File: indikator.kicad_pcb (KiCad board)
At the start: 2 copper layers, 125 x 52.5 mm, 104 parts, among them J1 Conn_01x02, Q1 AO3400A, Q10 AO3400A, Q11 AO3400A, Q12 AO3400A, Q13 AO3400A, Q14 AO3400A, Q15 AO3400A, Q16 AO3400A, Q17 AO3400A, Q18 AO3400A, Q19 AO3400A, Q2 AO3400A, Q20 AO3400A, Q21 AO3400A, Q22 AO3400A, Q23 AO3400A, Q24 AO3400A, Q3 AO3400A, Q4 AO3400A, Q5 AO3400A, Q6 AO3400A, Q7 AO3400A, Q8 AO3400A, Q9 AO3400A, U1 XIAO-ESP32-C3-SMD, U2 74HC595, U3 74HC595, U4 74HC595

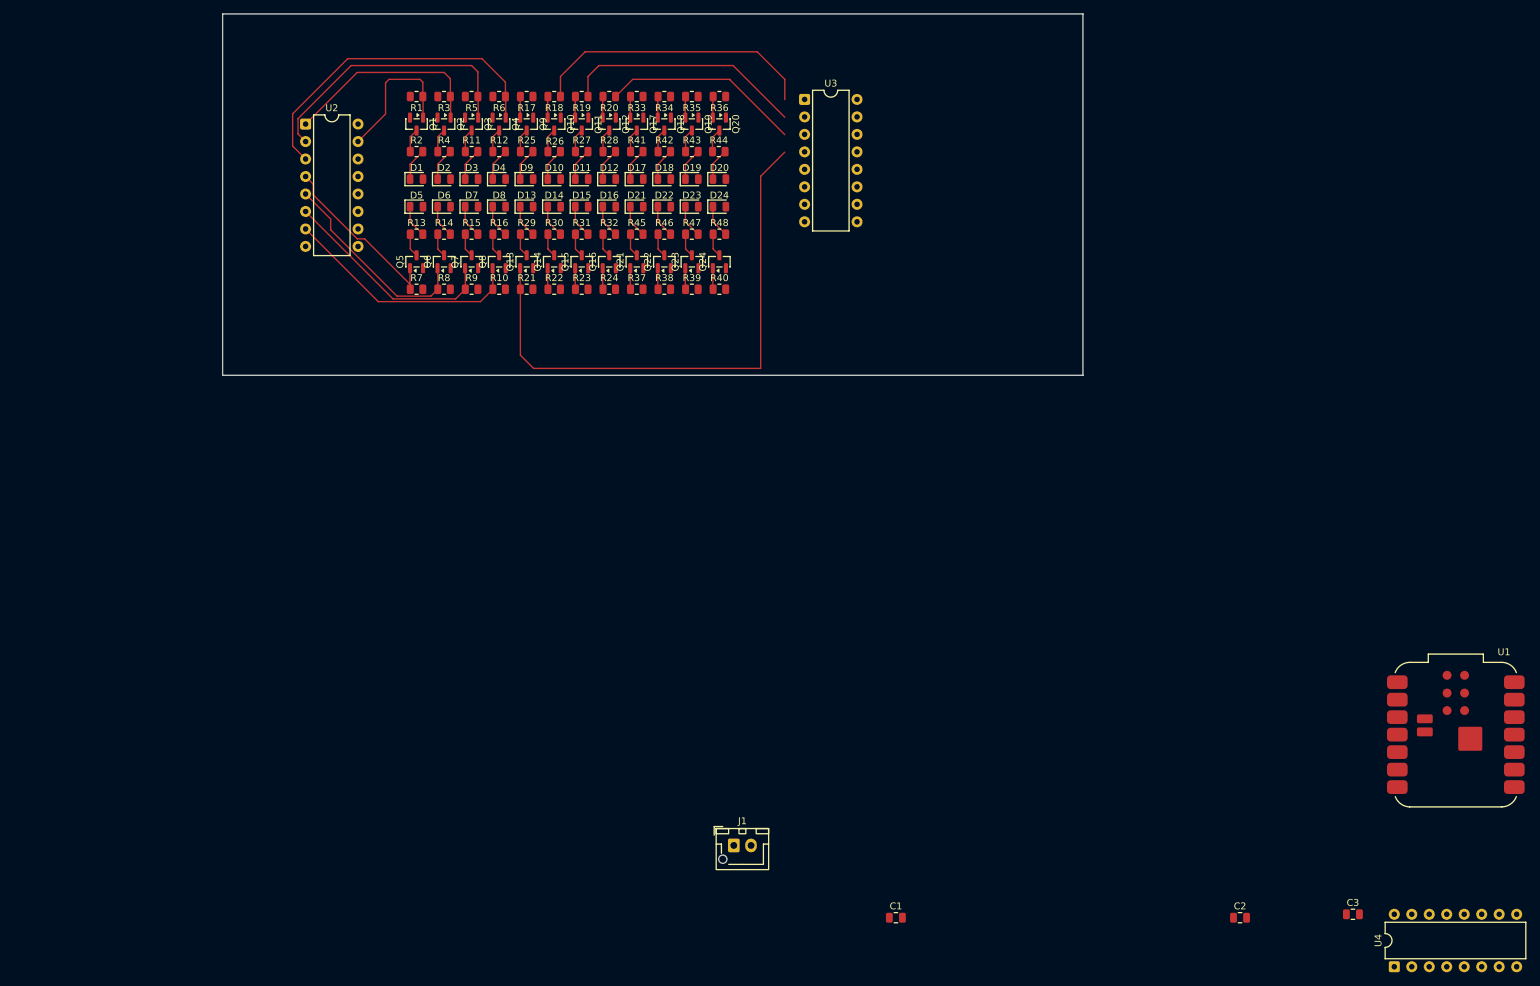
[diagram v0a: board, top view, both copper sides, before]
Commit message: LOTS of routing progress
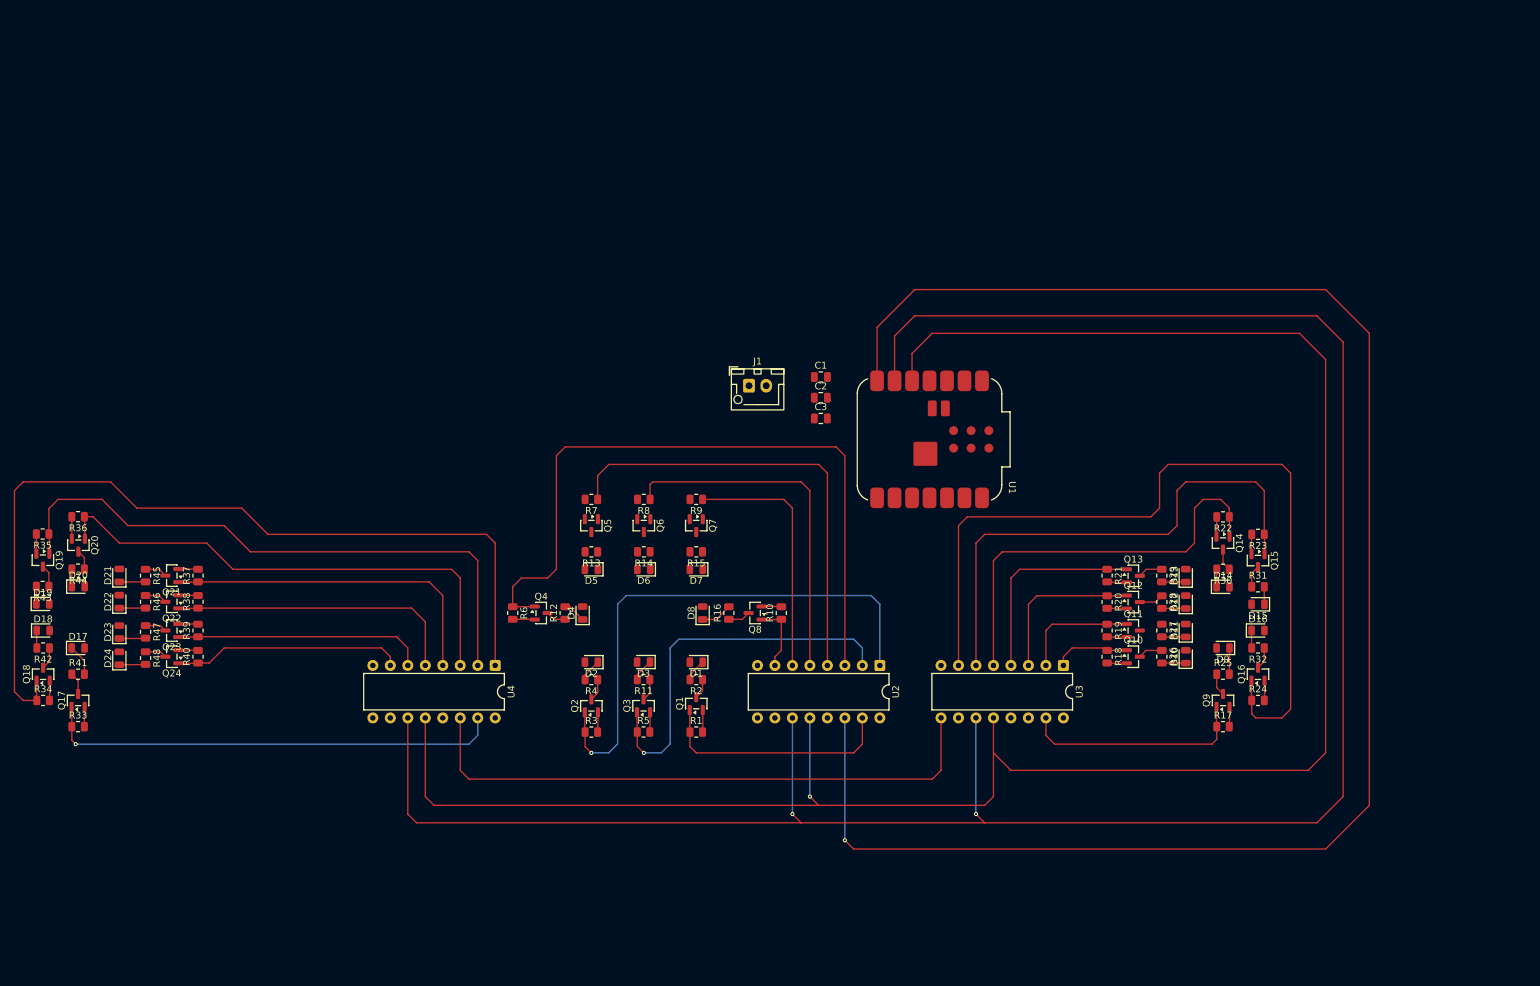
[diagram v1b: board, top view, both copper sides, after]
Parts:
- moved U4 137.8 mm to (116.6, 113.7), turned to -90 degrees
- moved R17 136.4 mm to (222.3, 122.5), turned to 0 degrees
- moved Q9 131.3 mm to (222.3, 118.7), turned to 90 degrees
- moved R25 126.5 mm to (222.3, 114.9)
- moved R34 125.9 mm to (50.9, 118.7), turned to 0 degrees
- moved R33 122.4 mm to (56.0, 122.5), turned to 0 degrees
- moved D9 122.0 mm to (222.3, 111.1), turned to 180 degrees
- moved Q18 120.6 mm to (50.9, 114.9), turned to 90 degrees
- moved Q17 116.6 mm to (56.0, 118.7), turned to 90 degrees
- moved R42 115.5 mm to (50.9, 111.1), turned to 180 degrees
- moved D10 115.0 mm to (216.9, 112.4), turned to 90 degrees
- moved R26 114.8 mm to (213.5, 112.4), turned to -90 degrees
- moved U2 114.7 mm to (172.5, 113.7), turned to -90 degrees
- moved R18 114.4 mm to (205.5, 112.4), turned to -90 degrees
- moved Q10 114.3 mm to (209.3, 112.4), turned to 0 degrees
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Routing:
- net /SRCLK: track 0.00 -> 324.0 mm, vias 0 -> 2
- net /RCLK: track 0.00 -> 294.1 mm, vias 0 -> 1
- net /SER: track 0.00 -> 249.9 mm, vias 0 -> 1
- net Net-(Q18-G): track 0.00 -> 127.7 mm
- net Net-(Q16-G): track 3.08 -> 121.3 mm
- net Net-(Q19-G): track 0.00 -> 88.4 mm
- net /QH'2: track 0.00 -> 86.1 mm
- net Net-(Q20-G): track 0.00 -> 74.3 mm
- net Net-(Q15-G): track 3.08 -> 76.1 mm
- net Net-(Q17-G): track 0.00 -> 67.1 mm, vias 0 -> 1
- net Net-(Q14-G): track 3.08 -> 60.9 mm
- net Net-(Q4-G): track 48.2 -> 103.5 mm
- net Net-(Q13-G): track 81.2 -> 30.1 mm
- net Net-(Q2-G): track 30.2 -> 79.7 mm, vias 0 -> 1
- net Net-(Q21-G): track 3.08 -> 49.4 mm
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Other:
- board outline removed

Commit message: kinda complete like you see the vision right
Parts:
- added REF**: MountingHole_3.2mm_M3, MountingHole:MountingHole_3.2mm_M3, F.Cu at (45.5, 66.7)
- added REF**: MountingHole_3.2mm_M3, MountingHole:MountingHole_3.2mm_M3, F.Cu at (45.5, 141.7)
- added REF**: MountingHole_3.2mm_M3, MountingHole:MountingHole_3.2mm_M3, F.Cu at (245.5, 141.7)
- added REF**: MountingHole_3.2mm_M3, MountingHole:MountingHole_3.2mm_M3, F.Cu at (245.5, 66.7)
- moved C1 29.8 mm to (181.0, 96.2), turned to -90 degrees
- moved C2 25.7 mm to (178.0, 96.2), turned to -90 degrees
- moved C3 21.5 mm to (175.0, 96.2), turned to -90 degrees
- moved U1 7.50 mm to (172.3, 79.5), turned to 180 degrees
- moved J1 4.05 mm to (150.0, 71.0)
- moved D1 1.28 mm to (145.8, 111.9)
- moved D10 1.28 mm to (216.9, 111.1)
- moved D12 1.28 mm to (216.9, 103.2)
- moved D13 1.28 mm to (216.9, 99.3)
- moved D14 1.28 mm to (222.3, 101.0)
- moved D17 1.28 mm to (56.0, 109.8)
- moved D19 1.28 mm to (50.9, 103.4)
- moved D2 1.28 mm to (130.6, 111.9)
- moved D20 1.28 mm to (56.0, 100.9)
- moved D21 1.28 mm to (62.0, 99.3)
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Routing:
- net /ESP3V3: track 0.00 -> 187.1 mm, vias 0 -> 2
- net /VBAT+: track 0.00 -> 89.2 mm, vias 0 -> 23
- net /QH'1: track 0.00 -> 81.1 mm, vias 0 -> 1
- net GND: track 61.6 -> 1.06 mm
- net /SER: track 249.9 -> 220.1 mm
- net /SRCLK: track 324.0 -> 300.6 mm
- net /RCLK: track 294.1 -> 275.7 mm
- net Net-(Q4-G): track 103.5 -> 98.3 mm
- net Net-(Q7-D): track 0.00 -> 3.25 mm
- net Net-(Q6-D): track 0.00 -> 3.25 mm
- net Net-(Q5-D): track 0.00 -> 3.25 mm
- net Net-(D7-K): track 0.00 -> 2.55 mm
- net Net-(D6-K): track 0.00 -> 2.55 mm
- net Net-(D5-K): track 0.00 -> 2.55 mm
- net Net-(Q5-G): track 66.0 -> 64.4 mm
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- added copper zone on B.Cu, net /VBAT+
- added copper zone on F.Cu, net GND
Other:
- board outline added: 210 x 85 mm

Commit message: fix all em errors
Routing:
- net GND: track 1.06 -> 69.2 mm, vias 0 -> 5
- net /VBAT+: track 89.2 -> 84.4 mm, vias 23 -> 25
- net Net-(Q11-D): track 0.00 -> 3.58 mm
- net Net-(Q2-G): track 79.7 -> 79.0 mm

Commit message: dis beautiful now
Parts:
- added G***: LOGO, LOGO, F.Cu at (74.7, 127.6)
- added G***: LOGO, LOGO, F.Cu at (92.5, 74.3)
- added G***: LOGO, LOGO, F.Cu at (105.2, 85.7)
- added G***: LOGO, LOGO, F.Cu at (216.9, 67.2)
- added G***: LOGO, LOGO, B.Cu at (147.1, 103.5)
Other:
- board text added: "> made for third space, a hack club ysws <"
